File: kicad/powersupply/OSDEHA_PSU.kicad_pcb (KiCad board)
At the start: 2 copper layers, 239.3 x 78.3 mm, 105 parts, among them J1 340 VAC / 220 mA, J2 340 VAC / 220 mA, J3 420 VAC / 75 mA, J4 9 VAC / 4.5 A, J5 Stator bias, J6 HV-L, J7 HV-R, J8 HEATERS-LEFT, J9 HEATERS-RIGHT, K1 RT424006, Q1 BD138, Q10 BC550, Q11 LND150, Q12 LND150, Q13 NTHL1000N170M1, Q14 BC550, Q2 10M90S, Q3 LND150, Q4 LND150, Q5 NTHL1000N170M1, Q6 BC550, Q7 LND150, Q8 LND150, Q9 NTHL1000N170M1, U1 LM1085-ADJ, U2 NE555P

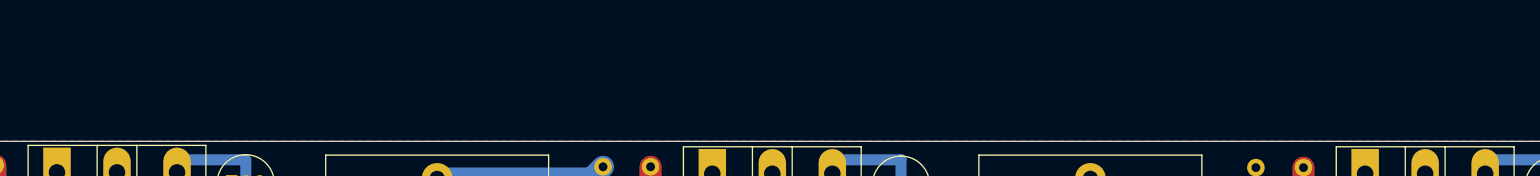
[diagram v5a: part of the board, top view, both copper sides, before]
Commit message: added Zener to clamp MOSFet VGS to 10 V
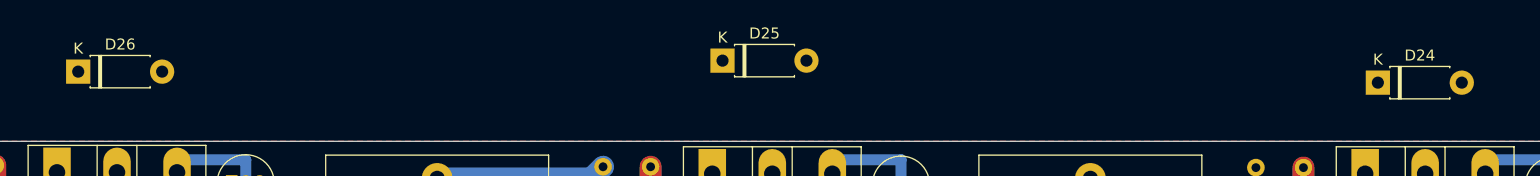
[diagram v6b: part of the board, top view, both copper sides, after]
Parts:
- added D24: 10 V, Diode_THT:D_DO-41_SOD81_P7.62mm_Horizontal, F.Cu at (230.2, 72.5)
- added D25: 10 V, Diode_THT:D_DO-41_SOD81_P7.62mm_Horizontal, F.Cu at (170.7, 70.5)
- added D26: 10 V, Diode_THT:D_DO-41_SOD81_P7.62mm_Horizontal, F.Cu at (112.2, 71.5)

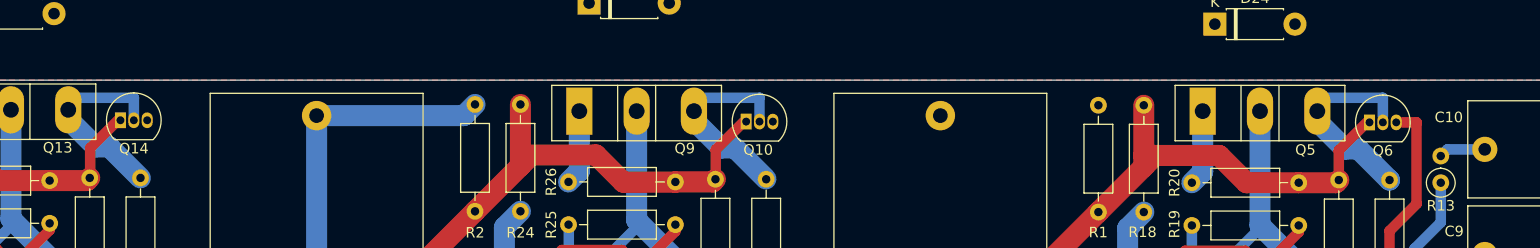
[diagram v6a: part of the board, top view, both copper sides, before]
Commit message: added base resistor for NPN BJT in current limiter
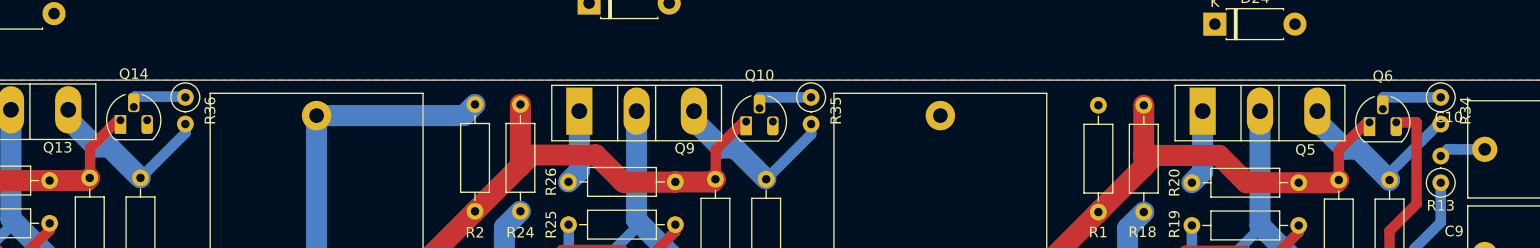
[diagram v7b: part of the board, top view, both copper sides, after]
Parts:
- added R34: 100, Resistor_THT:R_Axial_DIN0207_L6.3mm_D2.5mm_P2.54mm_Vertical, F.Cu at (251.7, 79.5)
- added R35: 100, Resistor_THT:R_Axial_DIN0207_L6.3mm_D2.5mm_P2.54mm_Vertical, F.Cu at (191.8, 79.5)
- added R36: 100, Resistor_THT:R_Axial_DIN0207_L6.3mm_D2.5mm_P2.54mm_Vertical, F.Cu at (132.3, 79.5)
- Q10, Q14, Q6: footprint Package_TO_SOT_THT:TO-92_Inline -> Package_TO_SOT_THT:TO-92_HandSolder
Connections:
- Q10 pad 2: Net-(D25-A) -> Net-(Q10-B)
- Q14 pad 2: Net-(D26-A) -> Net-(Q14-B)
- Q6 pad 2: Net-(D24-A) -> Net-(Q6-B)
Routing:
- net Net-(Q6-B): track 0.00 -> 5.52 mm
- net Net-(Q14-B): track 0.00 -> 4.97 mm
- net Net-(Q10-B): track 0.00 -> 4.92 mm
- net Net-(D26-A): track 16.9 -> 15.8 mm
- net Net-(D25-A): track 16.9 -> 15.9 mm
- net Net-(D24-A): track 17.1 -> 16.6 mm

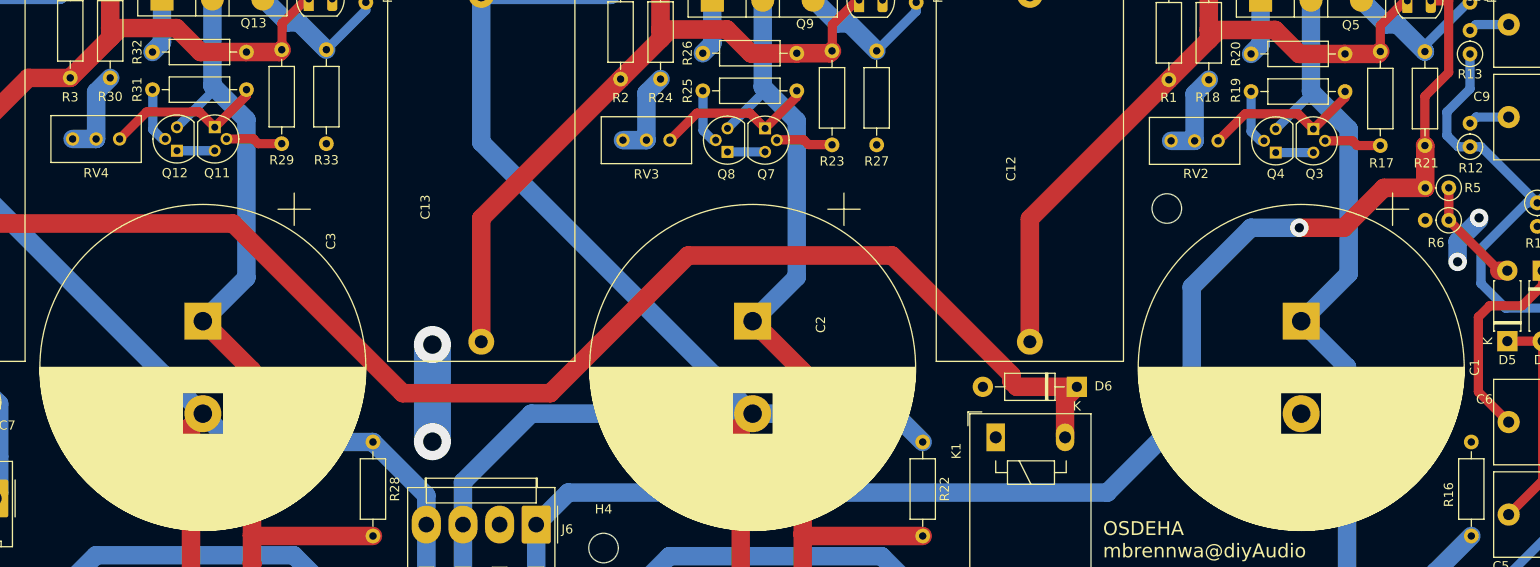
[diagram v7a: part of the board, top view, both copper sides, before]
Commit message: add dioded to outputs of HV supplies to prevent damage when loading outputs improperly
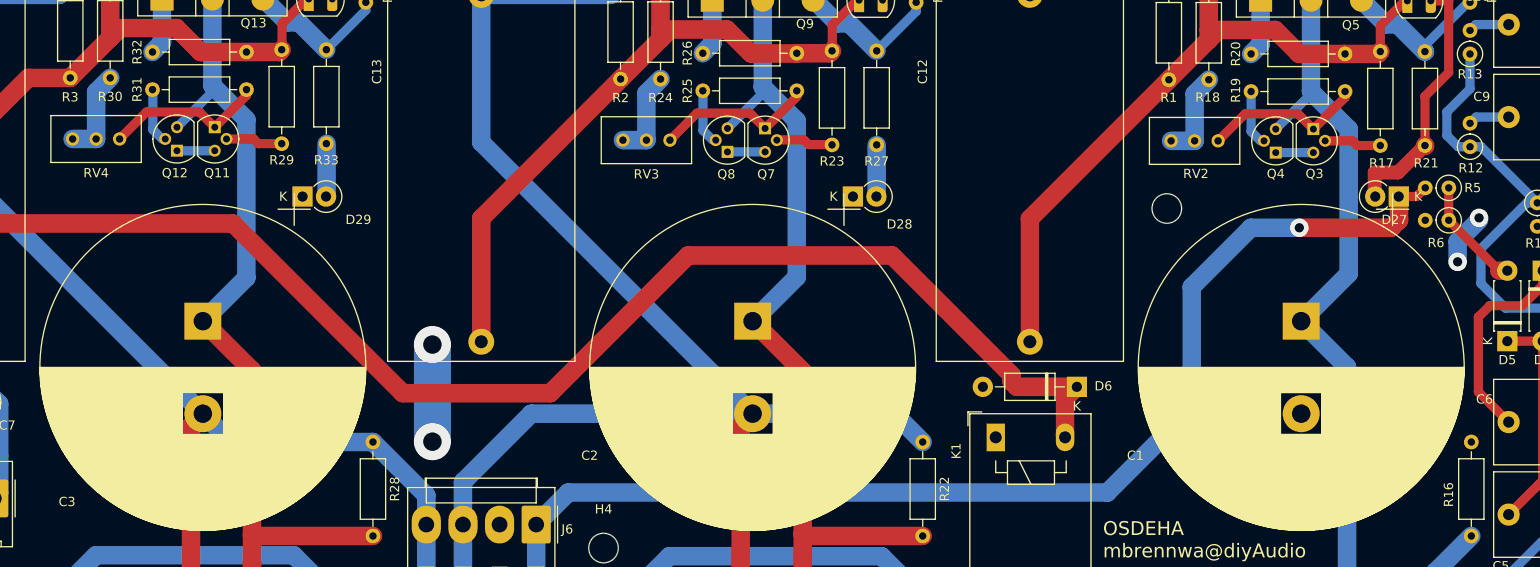
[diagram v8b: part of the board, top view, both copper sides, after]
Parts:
- added D27: 1N4007, Diode_THT:D_DO-41_SOD81_P2.54mm_Vertical_KathodeUp, F.Cu at (244.0, 103.0)
- added D28: 1N4007, Diode_THT:D_DO-41_SOD81_P2.54mm_Vertical_KathodeUp, F.Cu at (185.0, 103.0)
- added D29: 1N4007, Diode_THT:D_DO-41_SOD81_P2.54mm_Vertical_KathodeUp, F.Cu at (125.5, 103.0)
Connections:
- Q10 pad 3: GND -> Net-(D28-A)
- Q14 pad 3: GND -> Net-(D29-A)
- Q6 pad 3: /B+ -> Net-(D27-A)
- R21 pad 1: /B+ -> Net-(D27-A)
- R27 pad 1: GND -> Net-(D28-A)
- R33 pad 1: GND -> Net-(D29-A)
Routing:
- net Net-(D27-A): track 0.00 -> 27.4 mm
- net /B+: track 153.4 -> 132.2 mm
- net Net-(D28-A): track 0.00 -> 5.75 mm
- net Net-(D29-A): track 0.00 -> 5.73 mm
